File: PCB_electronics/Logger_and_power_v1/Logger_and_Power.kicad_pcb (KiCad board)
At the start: 2 copper layers, 41 parts, among them IC1 ATMEGA328-P, P1 SOLAR_PANEL, P10 CONN_01X08, P11 CONN_01X08, P12 CONN_01X03, P13 CONN_01X02, P14 CONN_01X02, P15 CONN_01X02, P2 5V_pololu, P3 BATT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

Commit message: routed ok
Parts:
- moved R9 7.50 mm to (167.5, 70.0)
- moved R8 5.00 mm to (177.5, 77.5)
- moved U4 2.50 mm to (172.5, 65.0)
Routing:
- net /Power_part/D5: track 0.00 -> 489.7 mm, vias 0 -> 3
- net +5V: track 0.00 -> 374.9 mm
- net /Power_part/Mega_ground: track 0.00 -> 204.7 mm
- net /Power_part/Batt_plus: track 0.00 -> 167.2 mm
- net /Logger_part/IRD_ON_OFF: track 0.00 -> 131.4 mm, vias 0 -> 6
- net /Power_part/Feedback_Mega: track 0.00 -> 120.5 mm
- net GND: track 0.00 -> 118.5 mm
- net /Logger_part/RPI_control: track 0.00 -> 94.8 mm, vias 0 -> 3
- net /Logger_part/MOSI: track 0.00 -> 89.2 mm, vias 0 -> 4
- net /Logger_part/SS: track 0.00 -> 77.4 mm, vias 0 -> 1
- net /Power_part/A1: track 0.00 -> 70.4 mm
- net /Logger_part/SCK: track 0.00 -> 69.5 mm, vias 0 -> 3
- net /Logger_part/MISO: track 0.00 -> 54.6 mm, vias 0 -> 1
- net /Power_part/D3: track 0.00 -> 53.7 mm
- net /Logger_part/MEGA_TX_1: track 0.00 -> 48.4 mm
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- added copper zone on F.Cu, net +5V
- added copper zone on B.Cu, net /Power_part/Mega_ground
- added copper zone on B.Cu, net GND
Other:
- board outline added: 97.5 x 90 mm
- net class Default: clearance 0.2 -> 0.3; trace_width 0.25 -> 0.3; via_dia 0.6 -> 0.7; via_drill 0.4 -> 0.5
- net class power added: clearance 0.3, trace_width 0.75, via_dia 0.9, via_drill 0.6
- rule trace_clearance: 0.2 -> 0.3

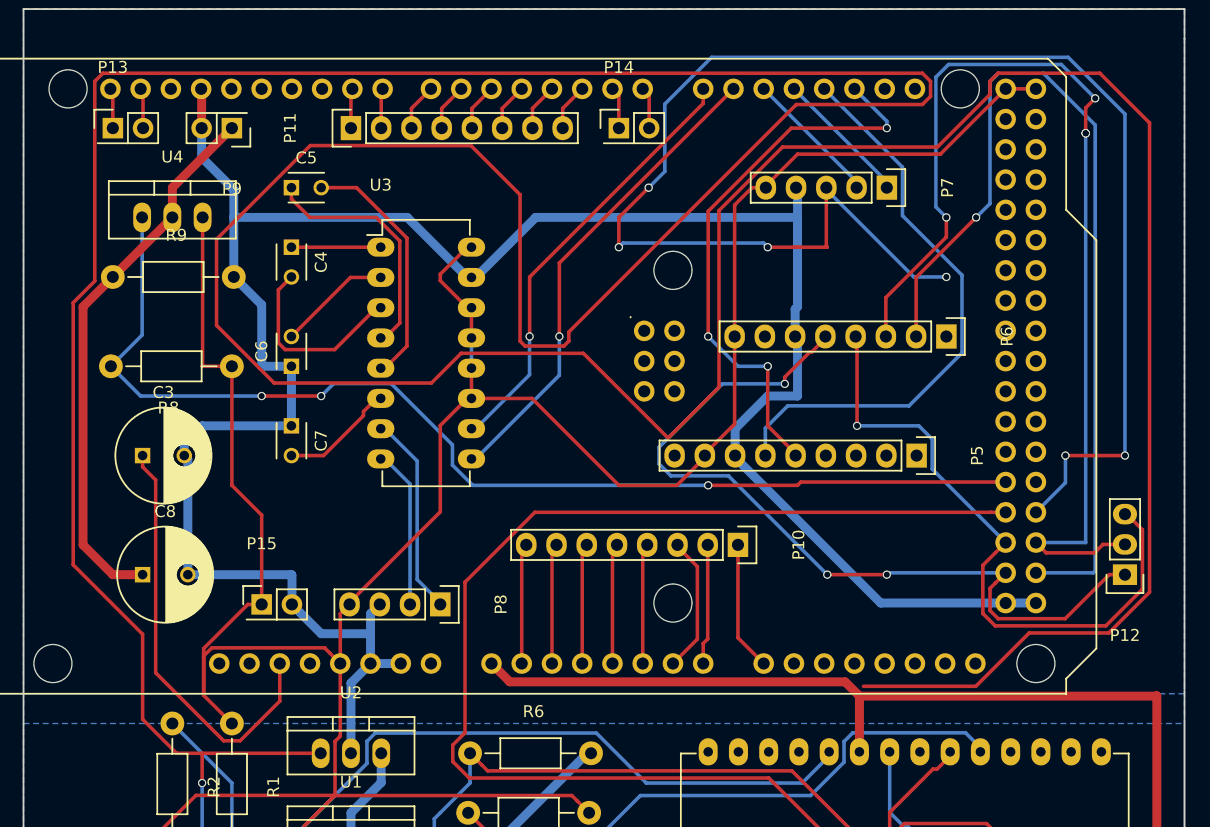
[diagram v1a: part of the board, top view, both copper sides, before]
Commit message: improved 5V plane
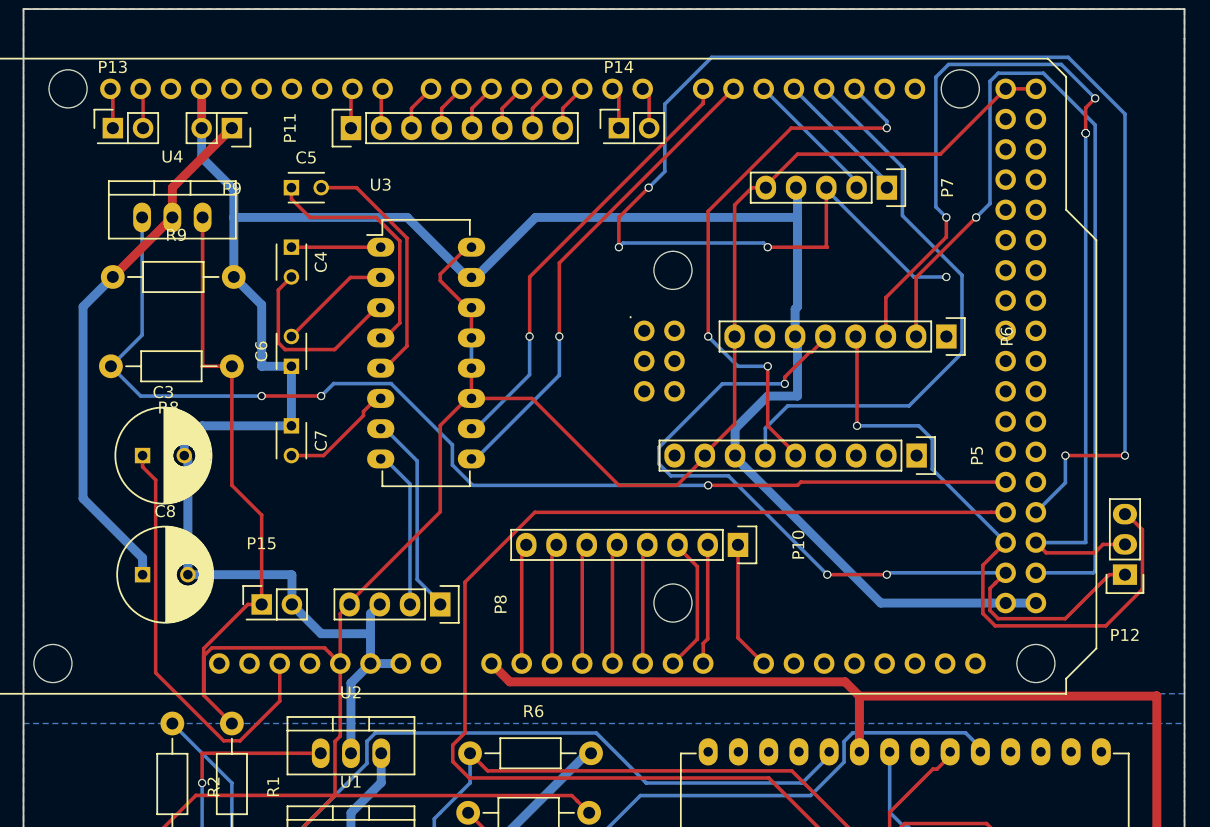
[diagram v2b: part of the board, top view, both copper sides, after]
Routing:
- net /Power_part/D5: track 489.7 -> 86.1 mm
- net Net-(C8-Pad1): track 46.2 -> 44.7 mm
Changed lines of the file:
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@@
     (thickness 1.6)
     (drawings 5)
-    (tracks 552)
+    (tracks 510)
     (zones 0)
     (modules 41)
@@
   (layers
     (0 F.Cu signal)
-    (31 B.Cu signal)
+    (31 B.Cu signal hide)
     (32 B.Adhes user hide)
     (33 F.Adhes user hide)
@@
   (segment (start 188.55 81.3) (end 189.65 80.2) (width 0.3) (layer F.Cu) (net 11))
   (segment (start 189.65 80.2) (end 190 80.2) (width 0.3) (layer F.Cu) (net 11))
-  (segment (start 167.5 70) (end 165 72.5) (width 0.75) (layer F.Cu) (net 12))
-  (segment (start 165 72.5) (end 165 92.5) (width 0.75) (layer F.Cu) (net 12))
-  (segment (start 165 92.5) (end 167.5 95) (width 0.75) (layer F.Cu) (net 12))
-  (segment (start 167.5 95) (end 170 95) (width 0.75) (layer F.Cu) (net 12))
+  (segment (start 167.5 70) (end 165 72.5) (width 0.75) (layer B.Cu) (net 12))
+  (segment (start 165 72.5) (end 165 88.6) (width 0.75) (layer B.Cu) (net 12))
+  (segment (start 165 88.6) (end 170 93.6) (width 0.75) (layer B.Cu) (net 12))
+  (segment (start 170 93.6) (end 170 95) (width 0.75) (layer B.Cu) (net 12))
   (segment (start 167.5 70) (end 172.5 65) (width 0.75) (layer F.Cu) (net 12))
   (segment (start 172.5 62.5) (end 172.5 65) (width 0.75) (layer F.Cu) (net 12))
@@
   (segment (start 227.5 120) (end 207.5 120) (width 0.3) (layer F.Cu) (net 18))
   (segment (start 227.66 117.5) (end 227.66 119.84) (width 0.3) (layer F.Cu) (net 18))
-  (segment (start 175 110) (end 172.854752 110) (width 0.3) (layer F.Cu) (net 19))
-  (segment (start 239.97384 104.37499) (end 230.54173 104.37499) (width 0.3) (layer F.Cu) (net 19))
-  (segment (start 165.983499 53.573071) (end 166.666571 52.889999) (width 0.3) (layer F.Cu) (net 19))
-  (segment (start 196.752229 76.40999) (end 207.011885 76.40999) (width 0.3) (layer F.Cu) (net 19))
-  (segment (start 172.854752 110) (end 170 107.145248) (width 0.3) (layer F.Cu) (net 19))
-  (segment (start 244.45161 99.89722) (end 239.97384 104.37499) (width 0.3) (layer F.Cu) (net 19))
-  (segment (start 201.699999 75.384001) (end 201.699999 63.090126) (width 0.3) (layer F.Cu) (net 19))
-  (segment (start 170 107.145248) (end 170 100) (width 0.3) (layer F.Cu) (net 19))
-  (segment (start 184.076438 58.96601) (end 176.210509 66.831939) (width 0.3) (layer F.Cu) (net 19))
-  (segment (start 176.210509 66.831939) (end 176.210509 74.065261) (width 0.3) (layer F.Cu) (net 19))
-  (segment (start 164.174991 94.174991) (end 164.174991 72.158269) (width 0.3) (layer F.Cu) (net 19))
-  (segment (start 201.699999 63.090126) (end 197.575883 58.96601) (width 0.3) (layer F.Cu) (net 19))
-  (segment (start 170 100) (end 164.174991 94.174991) (width 0.3) (layer F.Cu) (net 19))
-  (segment (start 235.491629 55.517201) (end 224.898799 55.517201) (width 0.3) (layer F.Cu) (net 19))
-  (segment (start 164.174991 72.158269) (end 165.983499 70.349761) (width 0.3) (layer F.Cu) (net 19))
-  (segment (start 165.983499 70.349761) (end 165.983499 53.573071) (width 0.3) (layer F.Cu) (net 19))
-  (segment (start 205.800001 74.615999) (end 205.800001 75.384001) (width 0.3) (layer F.Cu) (net 19))
-  (segment (start 254.56601 96.472134) (end 251.140924 99.89722) (width 0.3) (layer F.Cu) (net 19))
-  (segment (start 166.666571 52.889999) (end 235.491629 52.889999) (width 0.3) (layer F.Cu) (net 19))
-  (segment (start 194.252209 78.91001) (end 196.752229 76.40999) (width 0.3) (layer F.Cu) (net 19))
-  (segment (start 241.167499 53.573071) (end 241.850571 52.889999) (width 0.3) (layer F.Cu) (net 19))
-  (segment (start 197.575883 58.96601) (end 184.076438 58.96601) (width 0.3) (layer F.Cu) (net 19))
-  (segment (start 235.491629 52.889999) (end 236.174701 53.573071) (width 0.3) (layer F.Cu) (net 19))
-  (segment (start 241.850571 52.889999) (end 250.389999 52.889999) (width 0.3) (layer F.Cu) (net 19))
-  (segment (start 205.800001 75.384001) (end 205.384001 75.800001) (width 0.3) (layer F.Cu) (net 19))
-  (segment (start 236.174701 53.573071) (end 236.174701 54.834129) (width 0.3) (layer F.Cu) (net 19))
-  (segment (start 236.174701 54.834129) (end 235.491629 55.517201) (width 0.3) (layer F.Cu) (net 19))
-  (segment (start 224.898799 55.517201) (end 205.800001 74.615999) (width 0.3) (layer F.Cu) (net 19))
-  (segment (start 207.011885 76.40999) (end 214.135885 83.53399) (width 0.3) (layer F.Cu) (net 19))
-  (segment (start 223.740268 59.08759) (end 236.748568 59.08759) (width 0.3) (layer F.Cu) (net 19))
-  (segment (start 205.384001 75.800001) (end 202.115999 75.800001) (width 0.3) (layer F.Cu) (net 19))
-  (segment (start 202.115999 75.800001) (end 201.699999 75.384001) (width 0.3) (layer F.Cu) (net 19))
-  (segment (start 176.210509 74.065261) (end 181.055258 78.91001) (width 0.3) (layer F.Cu) (net 19))
-  (segment (start 181.055258 78.91001) (end 194.252209 78.91001) (width 0.3) (layer F.Cu) (net 19))
-  (segment (start 218.40639 64.421468) (end 223.740268 59.08759) (width 0.3) (layer F.Cu) (net 19))
-  (segment (start 214.135885 83.53399) (end 218.40639 79.263485) (width 0.3) (layer F.Cu) (net 19))
-  (segment (start 218.40639 79.263485) (end 218.40639 64.421468) (width 0.3) (layer F.Cu) (net 19))
-  (segment (start 254.56601 57.06601) (end 254.56601 96.472134) (width 0.3) (layer F.Cu) (net 19))
-  (segment (start 236.748568 59.08759) (end 241.167499 54.668659) (width 0.3) (layer F.Cu) (net 19))
-  (segment (start 241.167499 54.668659) (end 241.167499 53.573071) (width 0.3) (layer F.Cu) (net 19))
-  (segment (start 250.389999 52.889999) (end 254.56601 57.06601) (width 0.3) (layer F.Cu) (net 19))
-  (segment (start 251.140924 99.89722) (end 244.45161 99.89722) (width 0.3) (layer F.Cu) (net 19))
   (segment (start 184.96 110) (end 175 110) (width 0.3) (layer F.Cu) (net 19))
   (segment (start 175 112.5) (end 175 110) (width 0.3) (layer F.Cu) (net 19))

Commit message: ready to try to shift the power controller
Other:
- board size 97.5 x 90 mm -> 96.5 x 90 mm

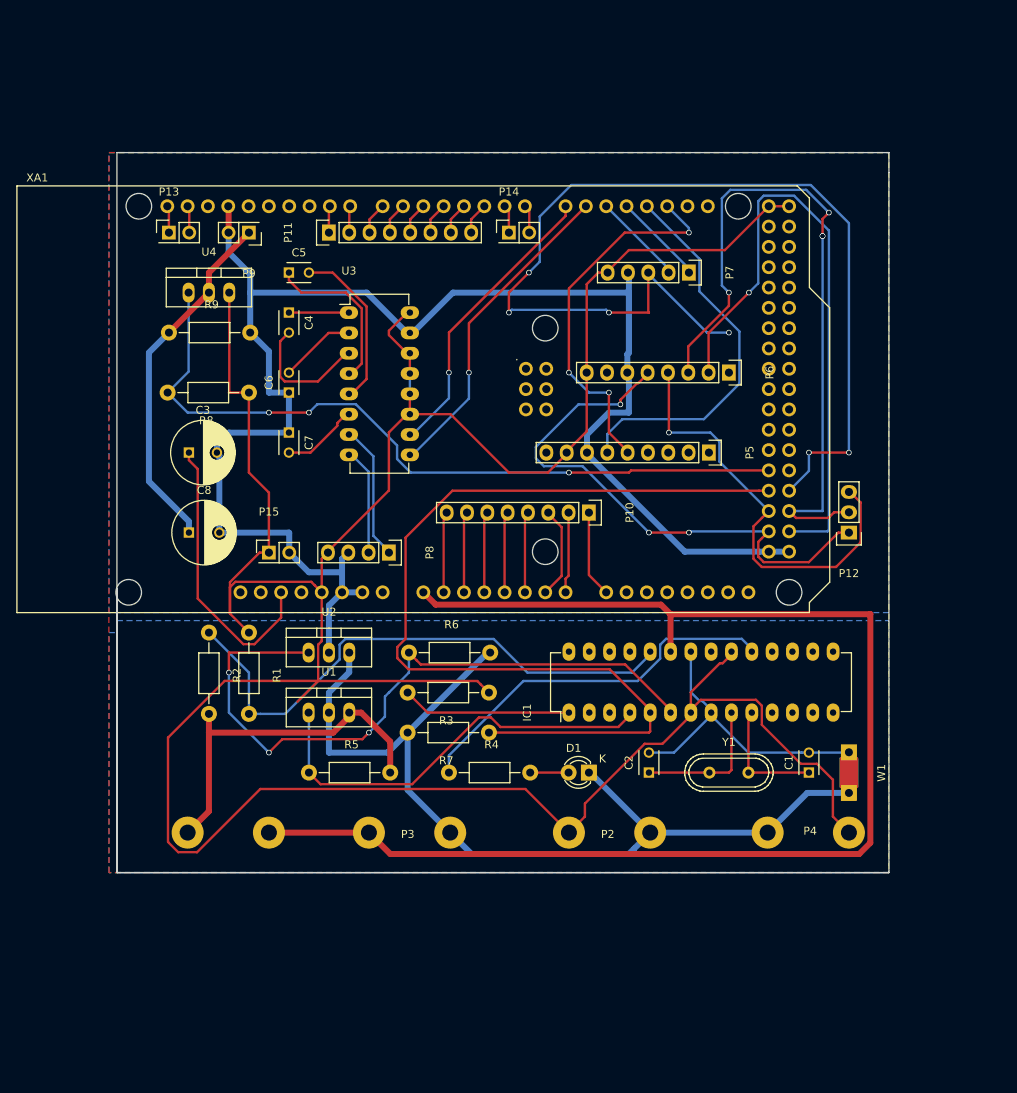
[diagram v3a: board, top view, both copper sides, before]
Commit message: moved more space for power controller
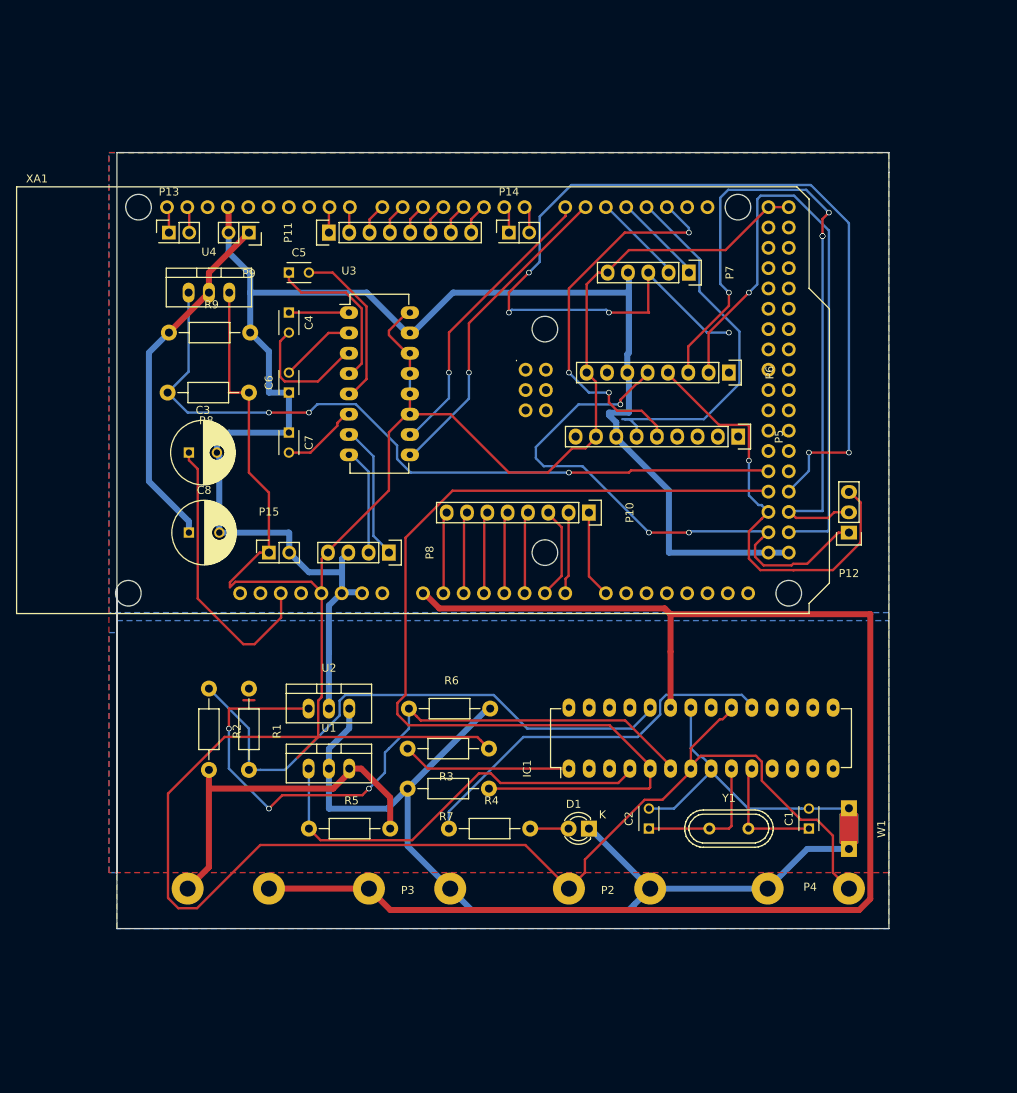
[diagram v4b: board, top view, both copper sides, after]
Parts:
- moved C1 7.00 mm to (247.5, 132.0)
- moved C2 7.00 mm to (227.5, 132.0)
- moved D1 7.00 mm to (220.0, 132.0)
- moved IC1 7.00 mm to (217.5, 124.5)
- moved P1 7.00 mm to (180.0, 139.5)
- moved P2 7.00 mm to (217.5, 139.5)
- moved P3 7.00 mm to (192.5, 139.5)
- moved P4 7.00 mm to (252.5, 139.5)
- moved R1 7.00 mm to (177.5, 114.5)
- moved R2 7.00 mm to (172.5, 114.5)
- moved R3 7.00 mm to (207.5, 122.0)
- moved R4 7.00 mm to (202.5, 132.0)
- moved R5 7.00 mm to (185.0, 132.0)
- moved R6 7.00 mm to (197.5, 117.0)
- moved R7 7.00 mm to (207.5, 127.0)
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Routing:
- net /Power_part/Batt_plus: track 167.2 -> 181.2 mm
- net /Power_part/Feedback_Mega: track 120.5 -> 127.5 mm
- net /Power_part/Mega_ground: track 204.7 -> 210.7 mm
- net /Logger_part/MEGA_TX_1: track 48.4 -> 46.6 mm
- net (no net): track 0.00 -> 1.39 mm
- net /Logger_part/MEGA_RX_1: track 47.3 -> 48.6 mm
- net +5V: track 374.9 -> 373.8 mm
- net /Logger_part/SCK: track 69.5 -> 70.4 mm
- net /Logger_part/MISO: track 54.6 -> 55.1 mm
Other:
- board size 96.5 x 90 mm -> 96.5 x 97 mm

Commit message: retablished 512bytes rx buffers; new PCB with logger and power and headers
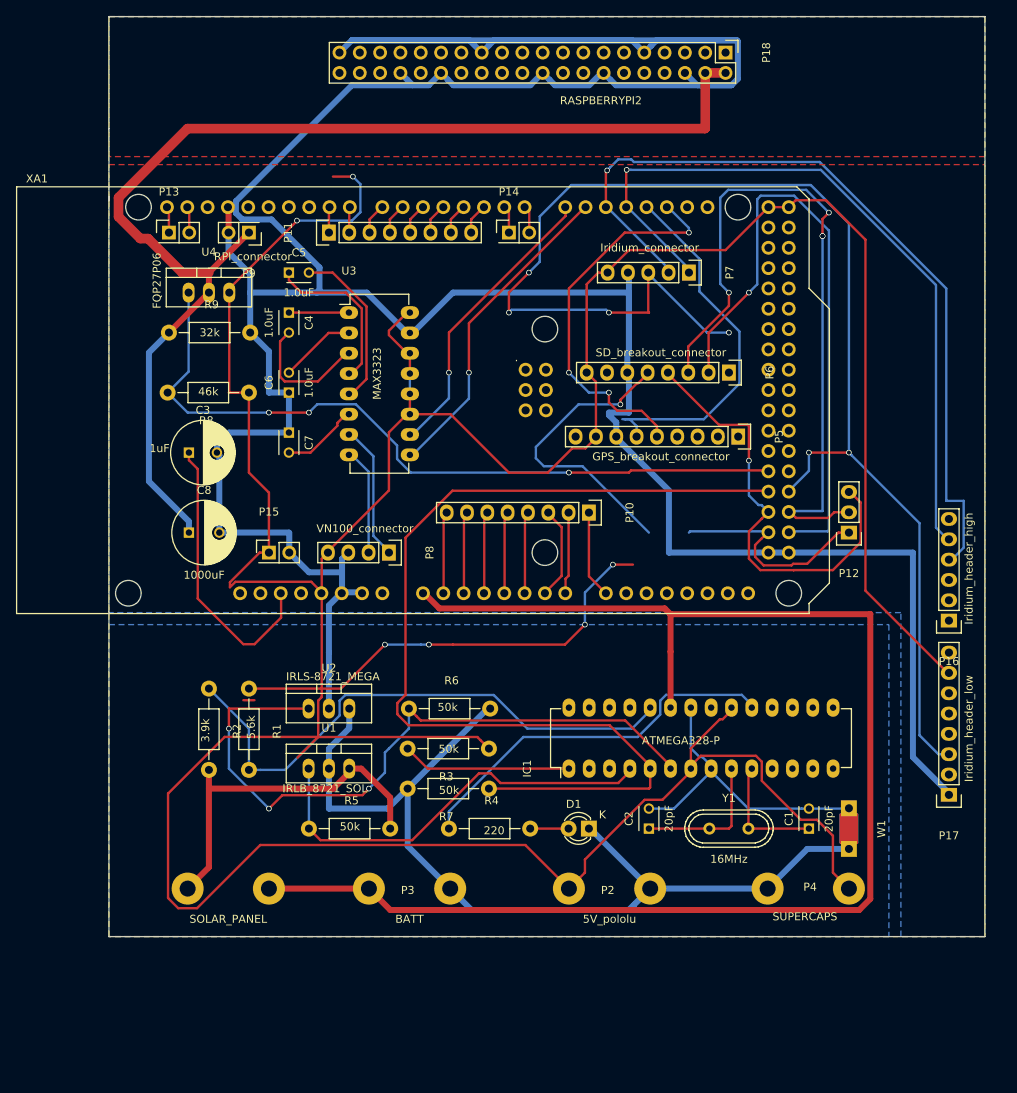
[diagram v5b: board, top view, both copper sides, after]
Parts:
- added P16: Iridium_header_high, Pin_Headers:Pin_Header_Straight_1x06, F.Cu at (265.0, 106.0)
- added P17: Iridium_header_low, Pin_Headers:Pin_Header_Straight_1x08, F.Cu at (265.0, 127.8)
- added P18: RASPBERRYPI2, Pin_Headers:Pin_Header_Straight_2x20, F.Cu at (237.1, 35.0)
- U3: value MAX232 -> MAX3323
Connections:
- net Net-(C8-Pad1) renamed /Logger_part/RPI_header/RPI_power_5V
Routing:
- net /Power_part/Mega_ground: track 210.7 -> 463.7 mm
- net +5V: track 373.8 -> 529.3 mm, vias 0 -> 6
- net /Logger_part/RPI_header/RPI_power_5V: track 44.7 -> 147.7 mm
- net /Logger_part/IRD_TXD: track 11.5 -> 105.5 mm, vias 0 -> 1
- net /Logger_part/IRD_RXC: track 11.5 -> 93.4 mm, vias 0 -> 1
- net /Logger_part/IRD_ON_OFF: track 131.4 -> 175.1 mm
- net /Logger_part/SCK: track 70.4 -> 65.4 mm, vias 3 -> 1
- added copper zone on F.Cu, net /Logger_part/RPI_header/RPI_power_5V
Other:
- board size 96.5 x 97 mm -> 109.5 x 115 mm
- net class large_power added: clearance 0.3, trace_width 1.2, via_dia 0.7, via_drill 0.5
- board text added: "Power and Logger with headers v1.0 Jean Rabault, UiO 05-2018"
